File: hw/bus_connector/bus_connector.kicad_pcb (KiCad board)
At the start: 2 copper layers, 68.7 x 35.4 mm, 11 parts, among them J1 DB9_Top, J2 DB9_Left, J3 DB9_Right

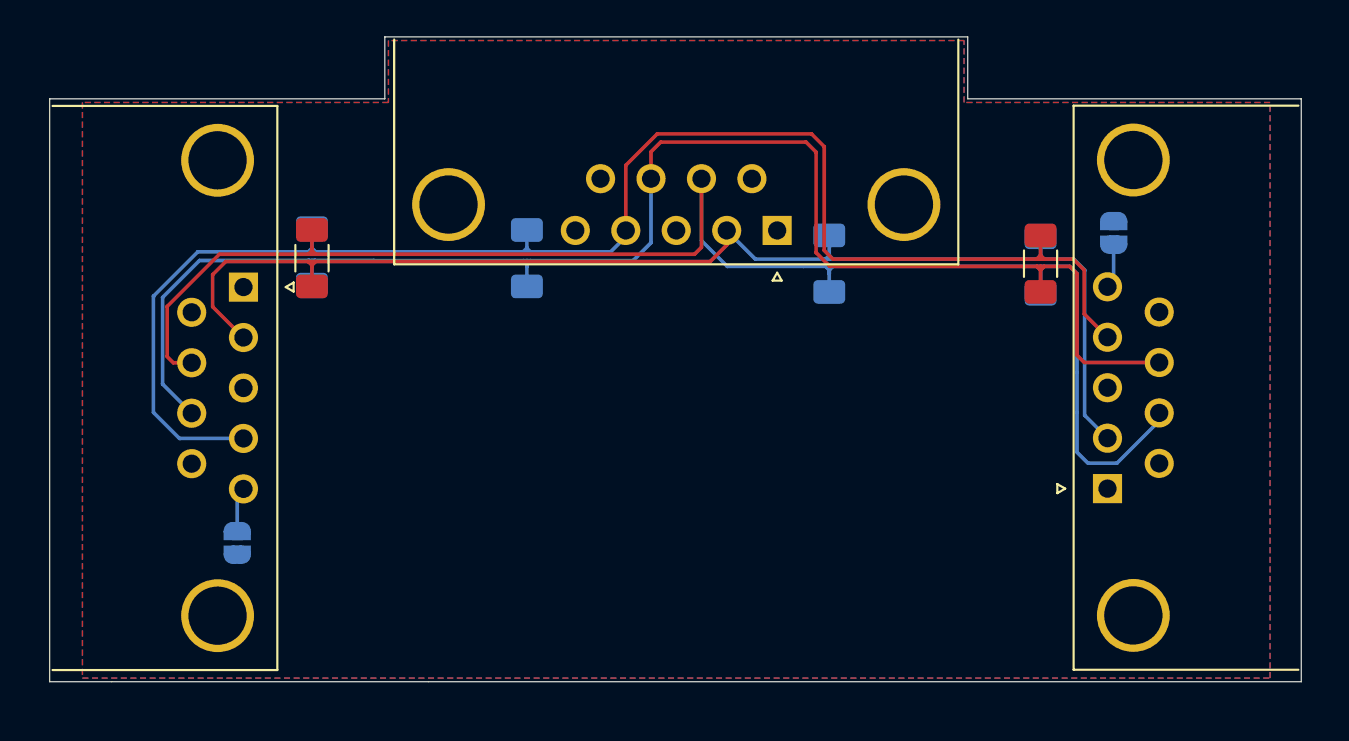
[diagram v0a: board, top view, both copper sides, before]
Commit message: Add test layout to connector PCB
Signed-off-by: Mateusz Pająk <22417805+Tai-Min@users.noreply.github.com>
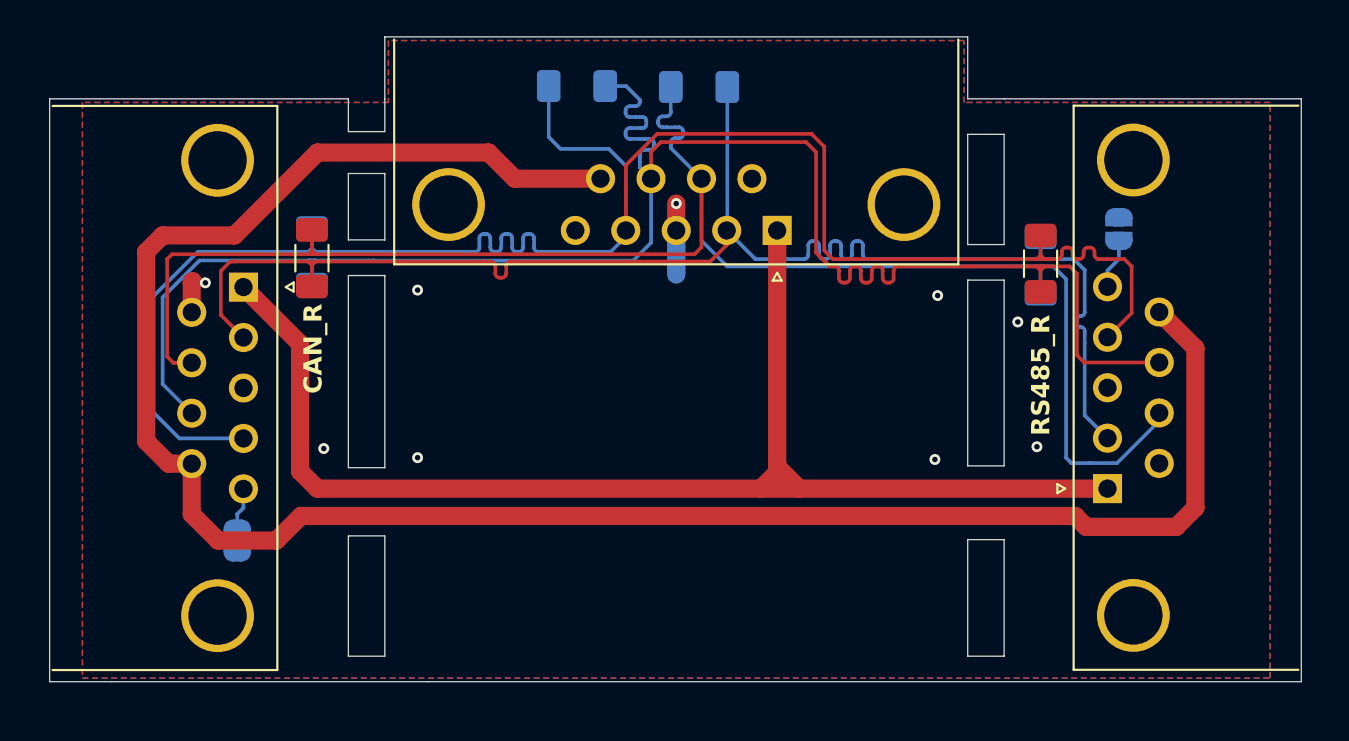
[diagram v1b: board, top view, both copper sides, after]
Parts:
- moved JP1 51.4 mm to (170.9, 98.8), turned to 90 degrees
- moved JP3 51.0 mm to (122.5, 115.8), turned to -90 degrees
- moved R2 12.1 mm to (147.8, 91.0), turned to 180 degrees
- moved R1 9.84 mm to (141.2, 90.9), turned to 0 degrees
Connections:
- J2 pad 5: SHIELD -> SHIELD_L
- J3 pad 5: SHIELD -> SHIELD_R
- JP1 pad 1: SHIELD -> SHIELD_L
- JP3 pad 1: SHIELD -> SHIELD_R
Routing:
- net VCC: track 0.00 -> 184.9 mm
- net MODBUS-: track 85.2 -> 103.6 mm
- net MODBUS+: track 85.0 -> 98.0 mm
- net CAN-: track 69.9 -> 81.7 mm
- net CAN+: track 85.9 -> 93.0 mm
- net GND: track 0.00 -> 5.64 mm, vias 0 -> 9
- net SHIELD: track 5.39 -> 0.00 mm
- net SHIELD_L: track 0.00 -> 3.26 mm
- net SHIELD_R: track 0.00 -> 2.81 mm
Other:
- outline, holes or cut-outs redrawn
- board text added: "CAN_R"
- board text added: "RS485_R"
- board text added: "SH"

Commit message: Edit actions
Signed-off-by: Mateusz Pająk <22417805+Tai-Min@users.noreply.github.com>
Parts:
- moved JP1 1.25 mm to (170.8, 100.0)
- moved R1 1.25 mm to (141.1, 92.2)
- moved J3 1.25 mm to (122.8, 103.2)
- moved JP3 1.25 mm to (122.5, 117.1)
- moved R3 1.25 mm to (126.5, 101.5)
- moved R4 1.25 mm to (126.5, 101.6)
- moved J1 1.25 mm to (152.1, 100.1)
- moved J2 1.25 mm to (170.2, 114.2)
- moved R2 1.25 mm to (147.8, 92.2)
- moved R5 1.25 mm to (166.6, 101.9)
- moved R6 1.25 mm to (166.6, 102.0)

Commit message: Fix issues with bus connector project
Signed-off-by: Mateusz Pająk <22417805+Tai-Min@users.noreply.github.com>
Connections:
- J1 pad 5: SHIELD -> unconnected-(J1-Pad5)
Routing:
- net VCC: track 184.9 -> 236.7 mm

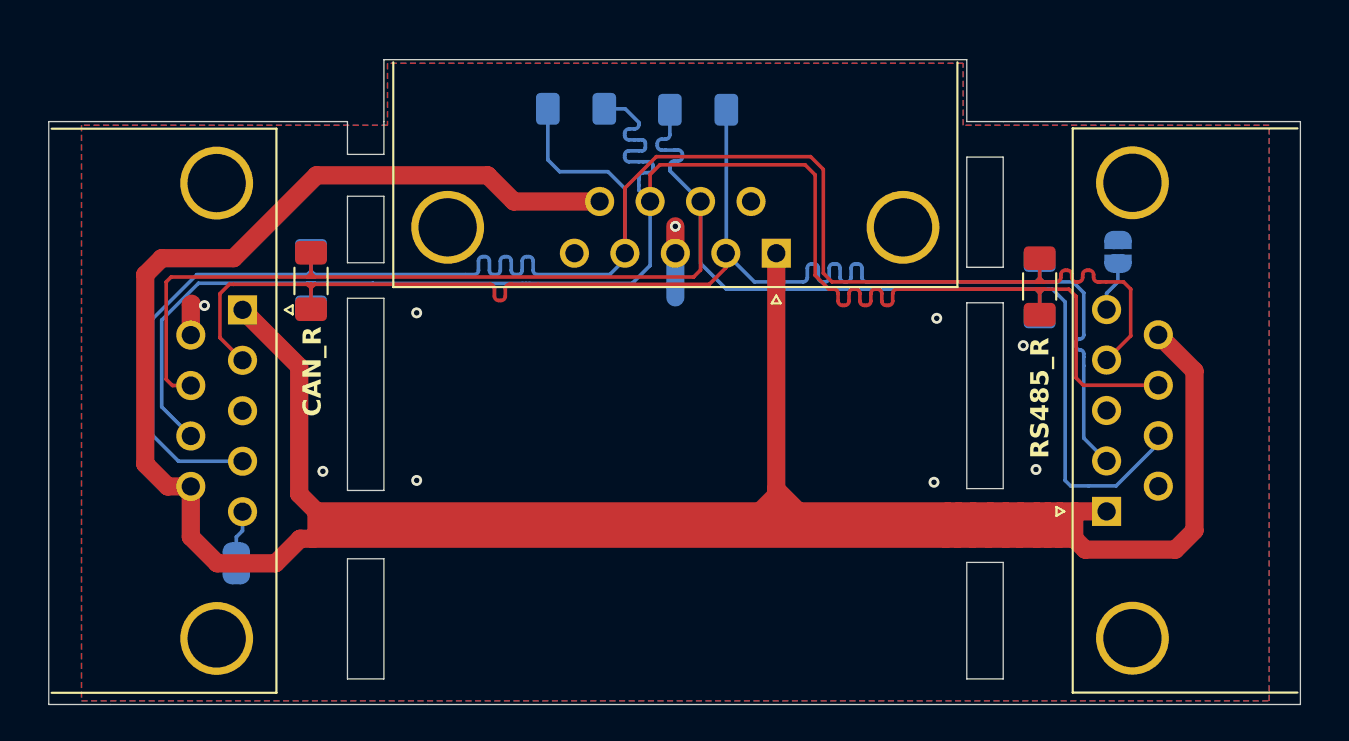
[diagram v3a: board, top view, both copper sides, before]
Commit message: Fix bus connector errors
Signed-off-by: Mateusz Pająk <22417805+Tai-Min@users.noreply.github.com>
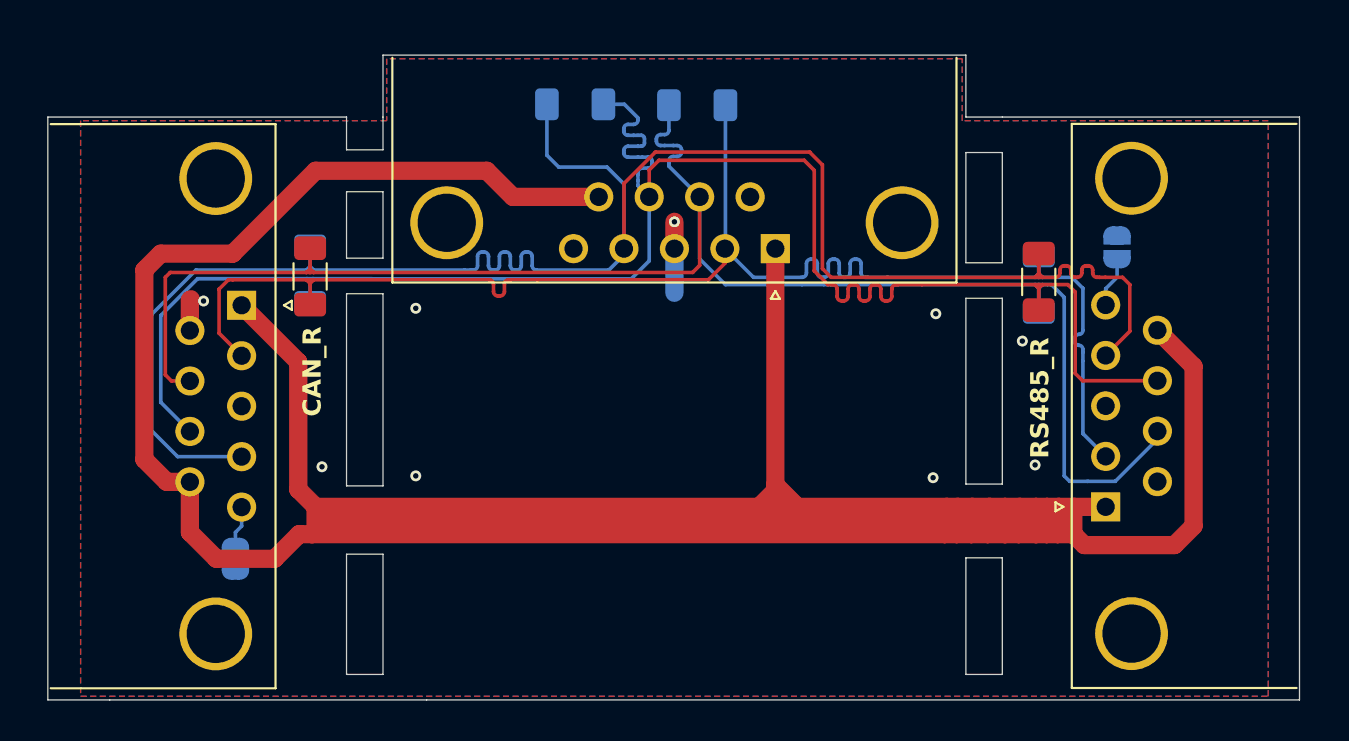
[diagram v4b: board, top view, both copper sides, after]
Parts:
- moved J1 0.25 mm to (152.0, 99.8)
- moved J2 0.25 mm to (170.2, 114.0)
- moved J3 0.25 mm to (122.7, 102.9)
- moved R2 0.25 mm to (147.8, 92.0)
- moved R5 0.25 mm to (166.5, 101.7)
- moved R6 0.25 mm to (166.5, 101.8)
- moved JP3 0.25 mm to (122.4, 116.8)
- moved R3 0.25 mm to (126.5, 101.2)
- moved R4 0.25 mm to (126.5, 101.3)
- moved JP1 0.25 mm to (170.8, 99.8)
- moved R1 0.25 mm to (141.1, 91.9)

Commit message: Finish bus connector prototype
Signed-off-by: Mateusz Pająk <22417805+Tai-Min@users.noreply.github.com>
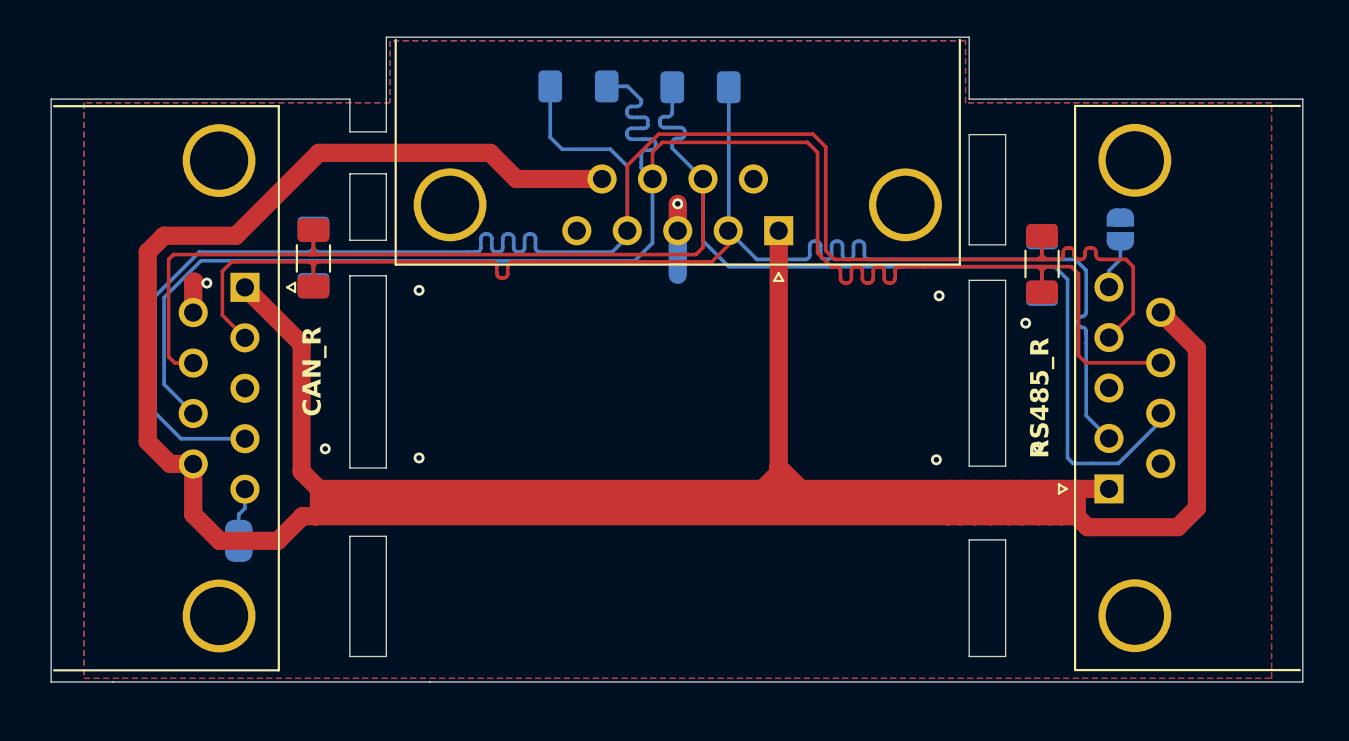
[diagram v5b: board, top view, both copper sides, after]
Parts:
- moved J1 1.00 mm to (152.2, 98.8)
- moved J2 1.00 mm to (170.4, 113.0)
- moved J3 1.00 mm to (122.9, 102.0)
- moved R3 1.00 mm to (126.7, 100.3)
- moved R4 1.00 mm to (126.7, 100.4)
- moved JP1 1.00 mm to (171.0, 98.8)
- moved JP3 1.00 mm to (122.6, 115.9)
- moved R1 1.00 mm to (141.2, 90.9)
- moved R2 1.00 mm to (147.9, 91.0)
- moved R5 1.00 mm to (166.7, 100.7)
- moved R6 1.00 mm to (166.7, 100.8)

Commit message: Simplify bus connector
Signed-off-by: Mateusz Pająk <22417805+Tai-Min@users.noreply.github.com>
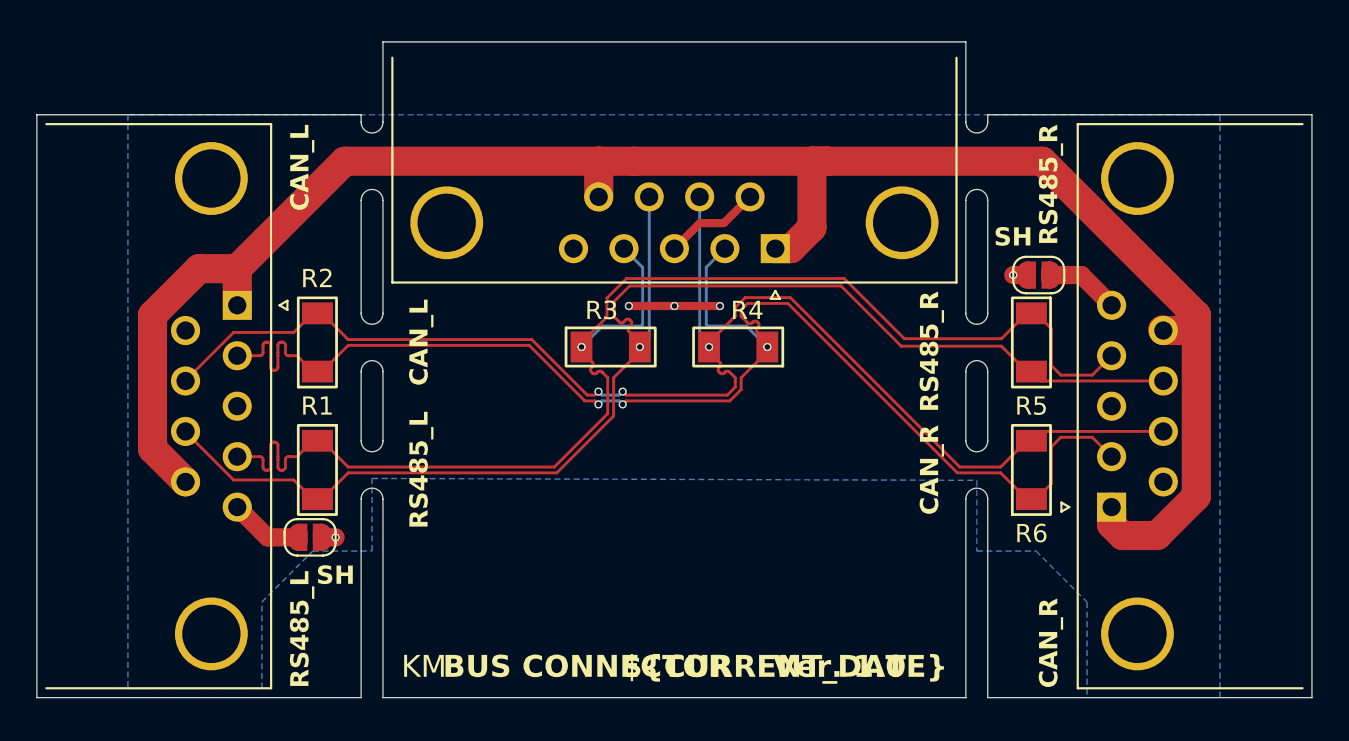
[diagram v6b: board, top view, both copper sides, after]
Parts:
- JP1, JP3: moved to F.Cu
- R1, R2, R3, R6: footprint Resistor_SMD:R_1206_3216Metric_Pad1.30x1.75mm_HandSolder -> KMur_kicad_lib:RLC_1206_3216Metric; moved to F.Cu
- R4, R5: footprint Resistor_SMD:R_1206_3216Metric_Pad1.30x1.75mm_HandSolder -> KMur_kicad_lib:RLC_1206_3216Metric
- moved R1 25.5 mm to (126.9, 112.0), turned to -90 degrees
- moved R2 25.3 mm to (126.9, 105.0), turned to 90 degrees
- moved R4 23.8 mm to (150.0, 105.2), turned to 180 degrees
- moved R3 17.1 mm to (143.0, 105.2), turned to 0 degrees
- moved R6 11.2 mm to (166.1, 112.0), turned to 90 degrees
- moved JP1 5.14 mm to (166.5, 101.3), turned to 180 degrees
- moved R5 4.35 mm to (166.1, 105.0)
- moved JP3 3.92 mm to (126.5, 115.7), turned to 0 degrees
- moved J3 1.07 mm to (122.5, 102.9)
- moved J2 1.01 mm to (170.5, 114.0)
- moved J1 1.00 mm to (152.0, 99.8)
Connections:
- net VCC renamed +24V
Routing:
- net +24V: track 236.7 -> 104.1 mm
- net MODBUS-: track 103.6 -> 75.8 mm, vias 0 -> 1
- net MODBUS+: track 98.0 -> 75.9 mm, vias 0 -> 1
- net CAN+: track 93.0 -> 76.7 mm, vias 0 -> 3
- net GND: track 5.64 -> 11.8 mm, vias 9 -> 5
- net CAN-: track 81.7 -> 76.7 mm, vias 0 -> 3
- net SHIELD_R: track 2.81 -> 4.04 mm
- net SHIELD_L: track 3.26 -> 4.04 mm
- removed copper zone on F.Cu, net GND
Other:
- board size 68.7 x 35.4 mm -> 70 x 36 mm
- board text added: "${CURRENT_DATE}"
- board text added: "${TITLE} Ver. ${REVISION}"
- board text added: "CAN_L"
- board text added: "KM"
- board text added: "RS485_L"
